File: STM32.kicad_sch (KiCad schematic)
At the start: 42 parts, among them IC201 ESDALC6V1W5, IC202 ESDALC6V1W5, IC203 ESDALC6V1W5, J1 Conn_01x04_Pin, J206 Conn_01x04_Pin, J207 Conn_01x07_Pin, Q201 DMG1012T-13, Q202 DMG1012T-13, Q203 DMG1012T-13, Q204 DMG1012T-13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

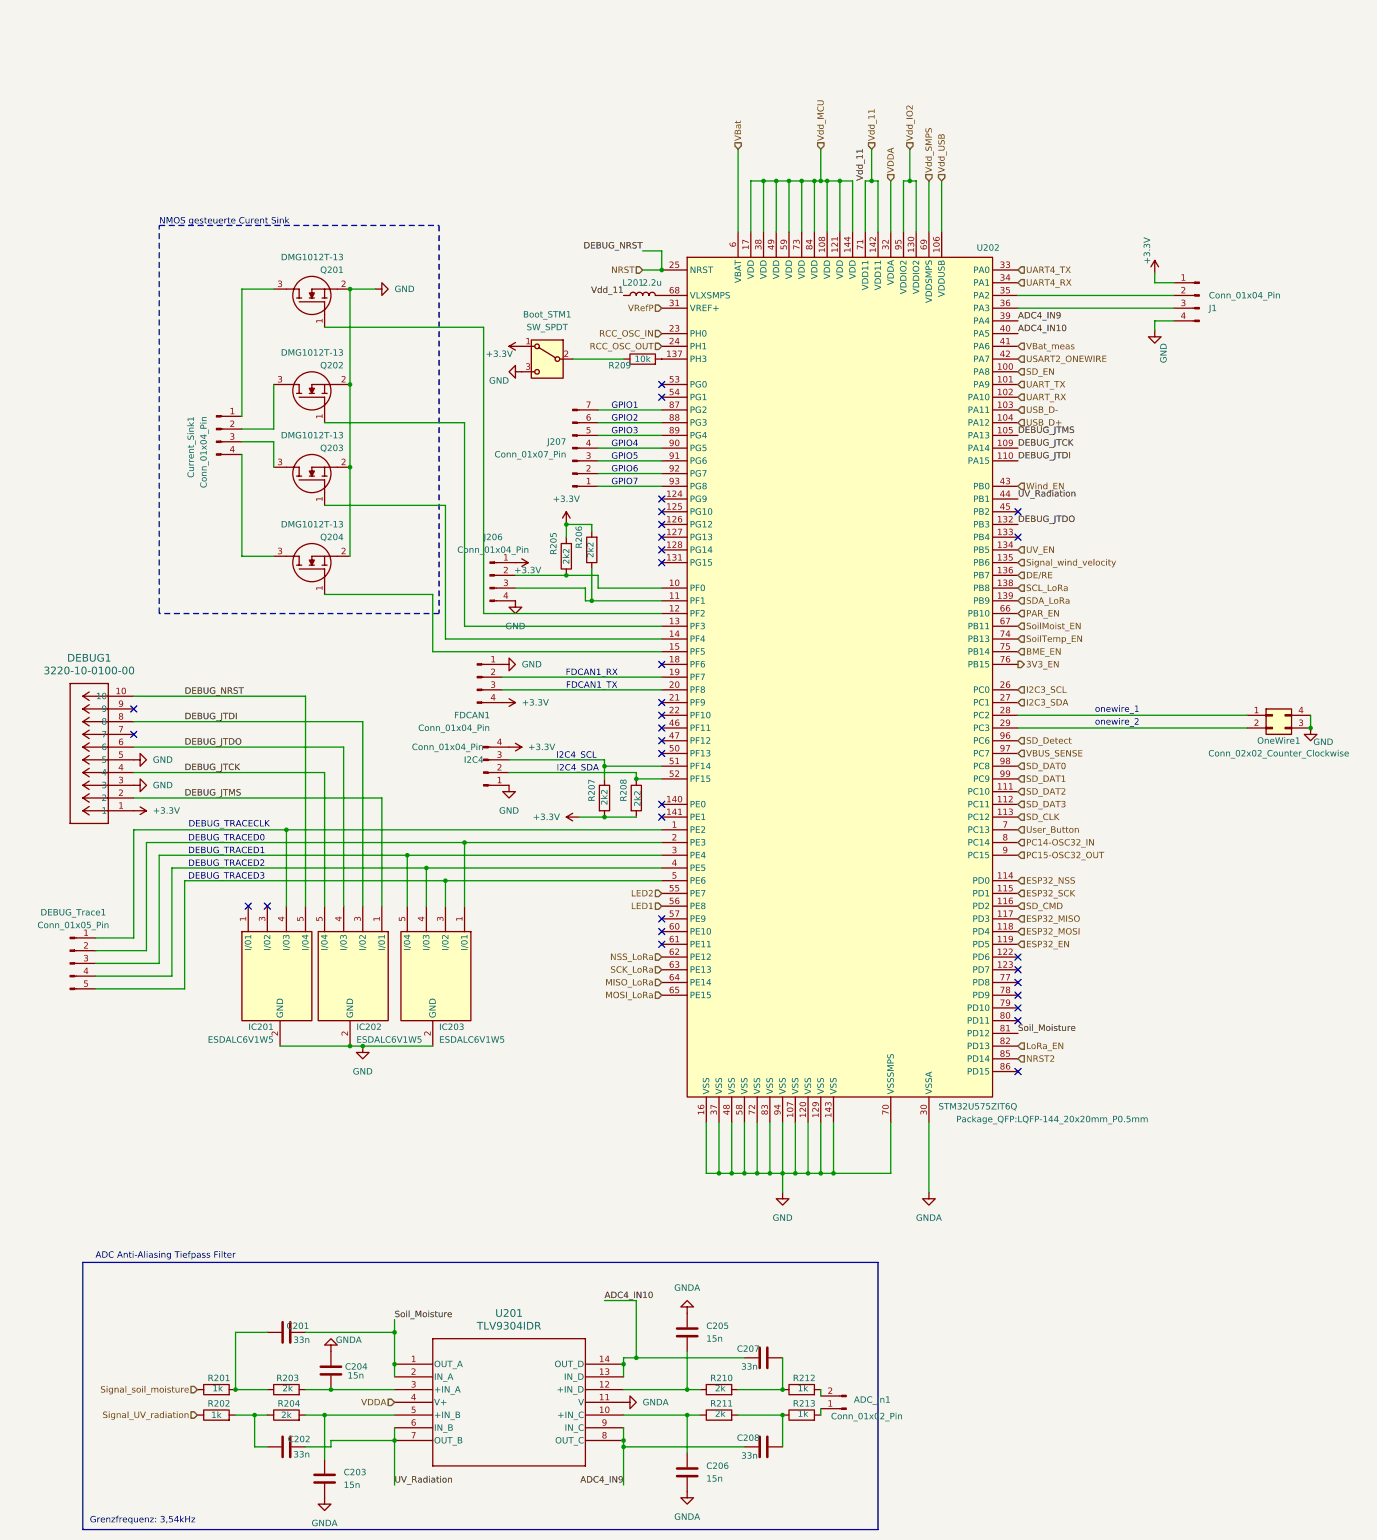
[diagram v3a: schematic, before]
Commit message: new layout
- recreation of the layout
- changed connection of ADC to MCU
- cleaner layout
- battery (supercap) for rtc
- crystal nearby the mcu
- 3V3 layer can be switched on/off separated from the mcu
- diode replaced with MOSFET
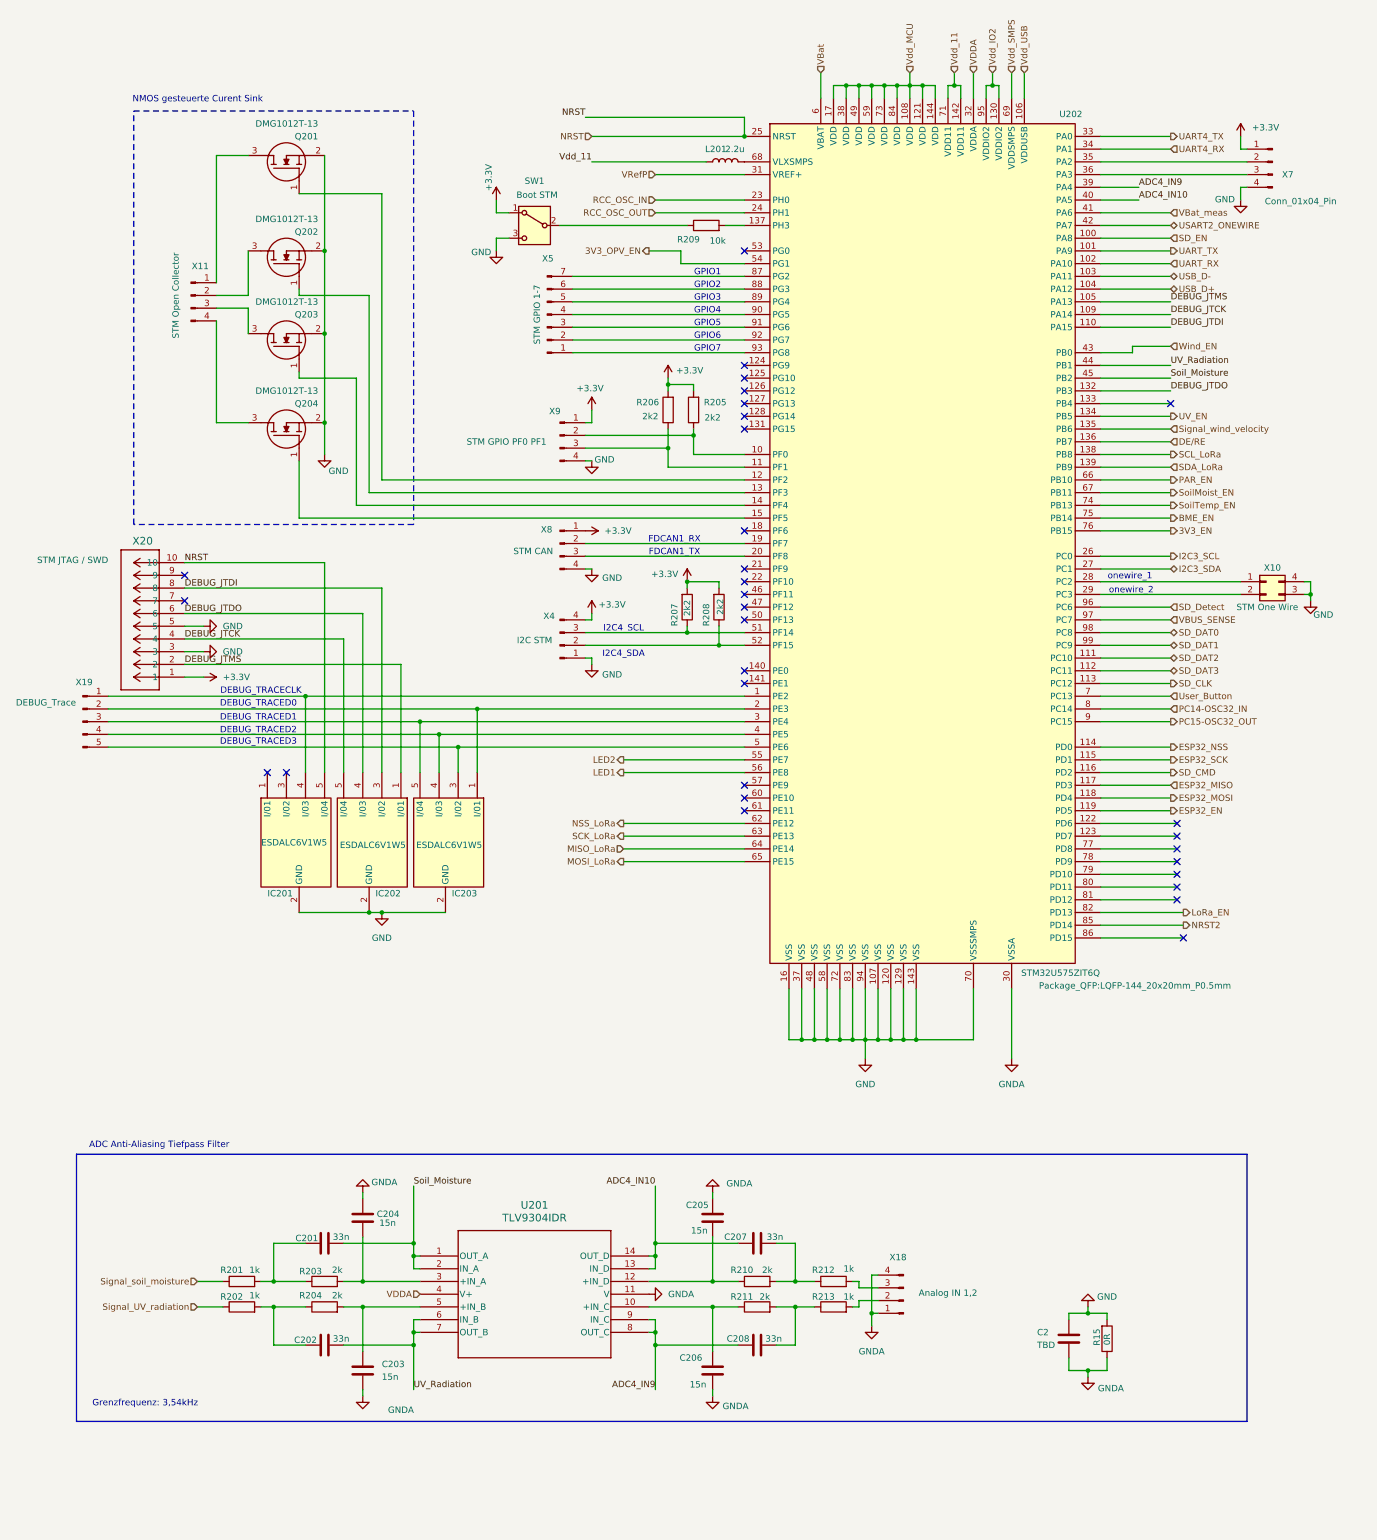
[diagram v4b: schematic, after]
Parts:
- removed ADC_In1: Conn_01x02_Pin, Connector_PinHeader_2.54mm:PinHeader_1x02_P2.54mm_Vertical, symbol Connector:Conn_01x02_Pin
- added C2: TBD, Capacitor_SMD:C_0805_2012Metric_Pad1.18x1.45mm_HandSolder, symbol Device:C
- added R15: 0R, Resistor_SMD:R_0805_2012Metric_Pad1.20x1.40mm_HandSolder, symbol Device:R
- added X18: Conn_01x04_Pin, Connector_JST:JST_XH_B4B-XH-AM_1x04_P2.50mm_Vertical, symbol Connector:Conn_01x04_Pin
- C203, C204, C205, C206: Mouser Part Number 80-C0805C153K1R -> 80-C0805C153K1R
- R203, R204, R210, R211: Mouser Part Number 667-ERJ-6ENF1001V -> 279-CRG0805F2K0
- U201: Mouser Part Number (none) -> 595-TLV9304IDR
- X10: renamed from OneWire1; Mouser Part Number (none) -> 649-67997-100HLF
- X11: renamed from Current_Sink1; Mouser Part Number (none) -> 523-G800LW304032EU
- X19: renamed from DEBUG_Trace1; Mouser Part Number (none) -> 523-G800W303018EU
- X4: renamed from I2C4; Mouser Part Number (none) -> 523-G800LW304032EU
- X5: renamed from J207; Mouser Part Number (none) -> 855-M20-9770746
- X7: renamed from J1; Mouser Part Number (none) -> 523-G800LW304032EU
- X8: renamed from FDCAN1; Mouser Part Number (none) -> 523-G800LW304032EU
- X9: renamed from J206; Mouser Part Number (none) -> 523-G800LW304032EU
- renumbered Boot_STM1 to SW1, DEBUG1 to X20
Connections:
- net +3.3V: now also X8.1 (Pin_1); no longer X8.4 (Pin_4)
- net GND: now also X8.4 (Pin_4), C2.2, R15.2; no longer X8.1 (Pin_1)
- net GNDA: now also C2.1, R15.1, X18.1 (Pin_1), X18.4 (Pin_4)
- net Soil_Moisture: now also U202.45 (PB2); no longer U202.81 (PD12)
- net at R212.2: now also X18.3 (Pin_3)
- net 3V3_OPV_EN: now reaches U202.54 (PG1)
- net at R213.2: now also X18.2 (Pin_2)
- no-connect marks 32 -> 31
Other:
- moved on the sheet: C201, C202, C203, C204, C205, C206, C207, C208, IC201, IC202, IC203, L201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
